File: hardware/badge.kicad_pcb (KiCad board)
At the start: 2 copper layers, 88 x 156.6 mm, 130 parts, among them J1 Micro_SD_Card, J2 MY-18650-01, J3 Conn_01x40, J4 USB_C_Receptacle_USB2.0_14P, J5 MY-18650-01, Q1 AO3400A, Q3 AO3400A, SW1 SW_Push, SW10 SW_Push, SW11 SW_Push, SW12 SW_Push, SW13 SW_Push, SW14 SW_Push, SW15 SW_Push, SW16 SW_Push, SW17 SW_Push, SW18 SW_Push, SW19 SW_Push, SW2 SW_Push, SW20 SW_Push, SW21 SW_Push, SW22 SW_Push, SW23 SW_Push, SW25 SW_Push, SW26 SW_Push, SW27 SW_Push, SW28 SW_Push, SW29 SW_Push, SW3 SW_Push, SW30 SW_Push, SW31 SW_Push, SW33 SW_Push, SW34 SW_Push, SW35 SW_Push, SW36 SW_Push, SW37 SW_Push, SW38 SW_Push, SW39 SW_Push, SW4 SW_Push, SW5 SW_Push, SW57 MK-12C02-G020, SW58 SKRHABE010, SW6 SW_Push, SW7 SW_Push, SW8 BOOT, SW9 SW_Push, U1 ESP32-S3-WROOM-1, U10 PCA9555PW, U11 PCA9555PW, U3 BQ24075RGT, U4 TLV62569DBV, U5 BME280, U6 USBLC6-2P6, U7 BMI270, U8 Ai-Thinker-Ra-02, U9 MAX98357A

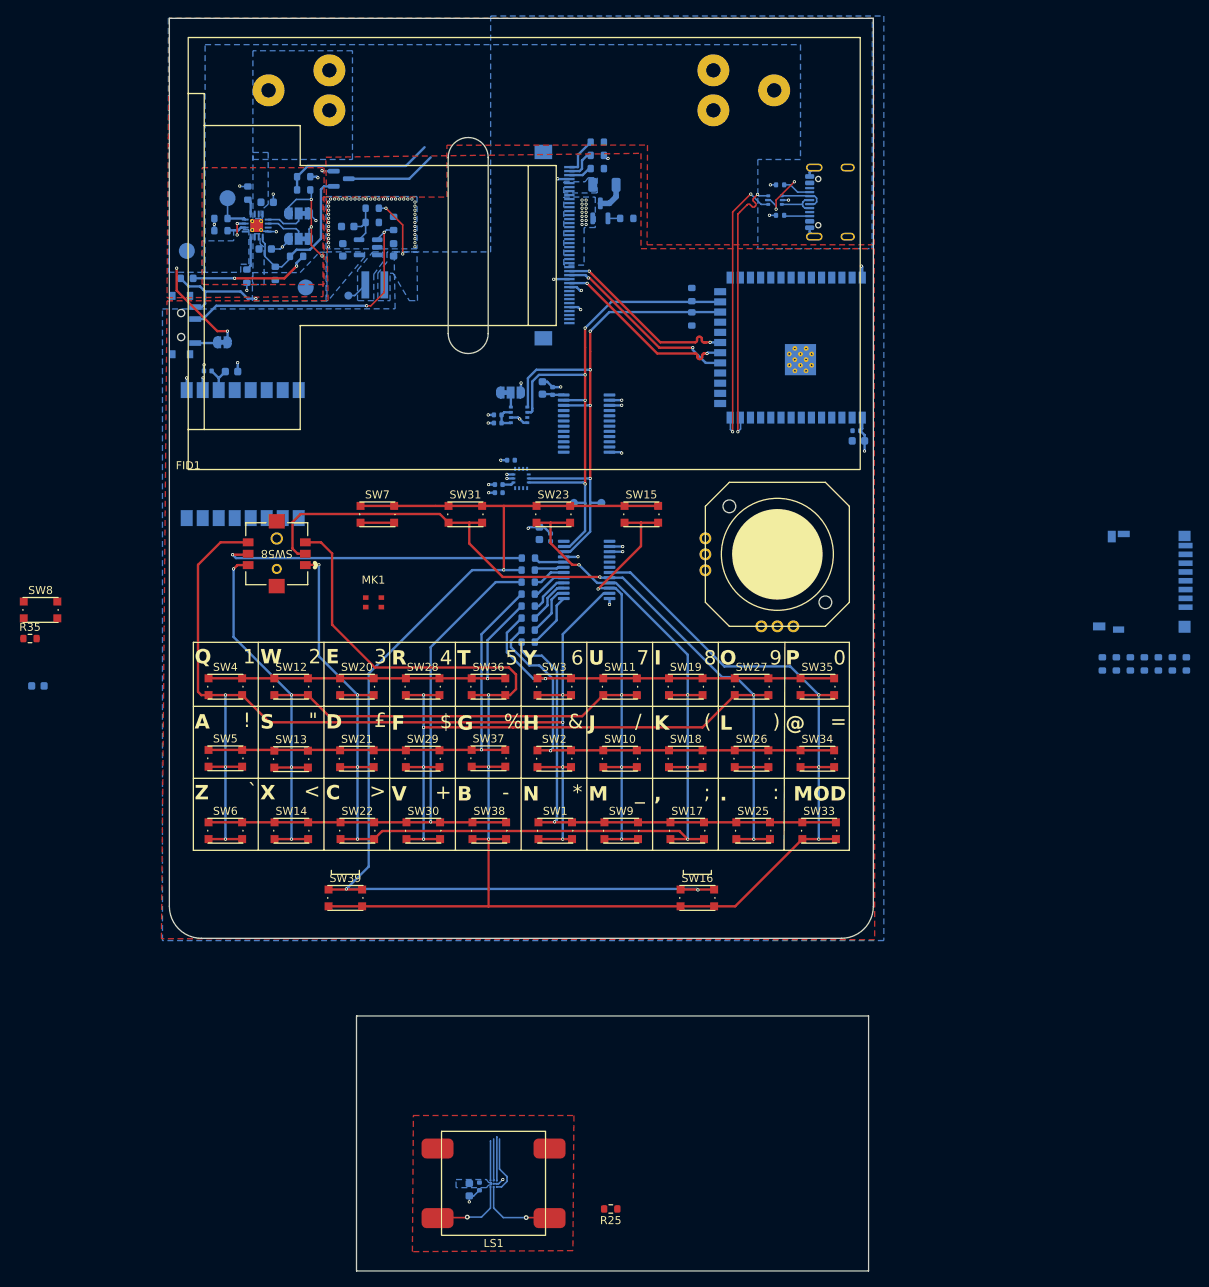
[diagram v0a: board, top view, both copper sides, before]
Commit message: Add sdcard fooprint
Remove io expander
Reorganize a bit the mcu schematic
Routed audio
Routed lora
Partial pin swapping of esp32 for facilitating routing
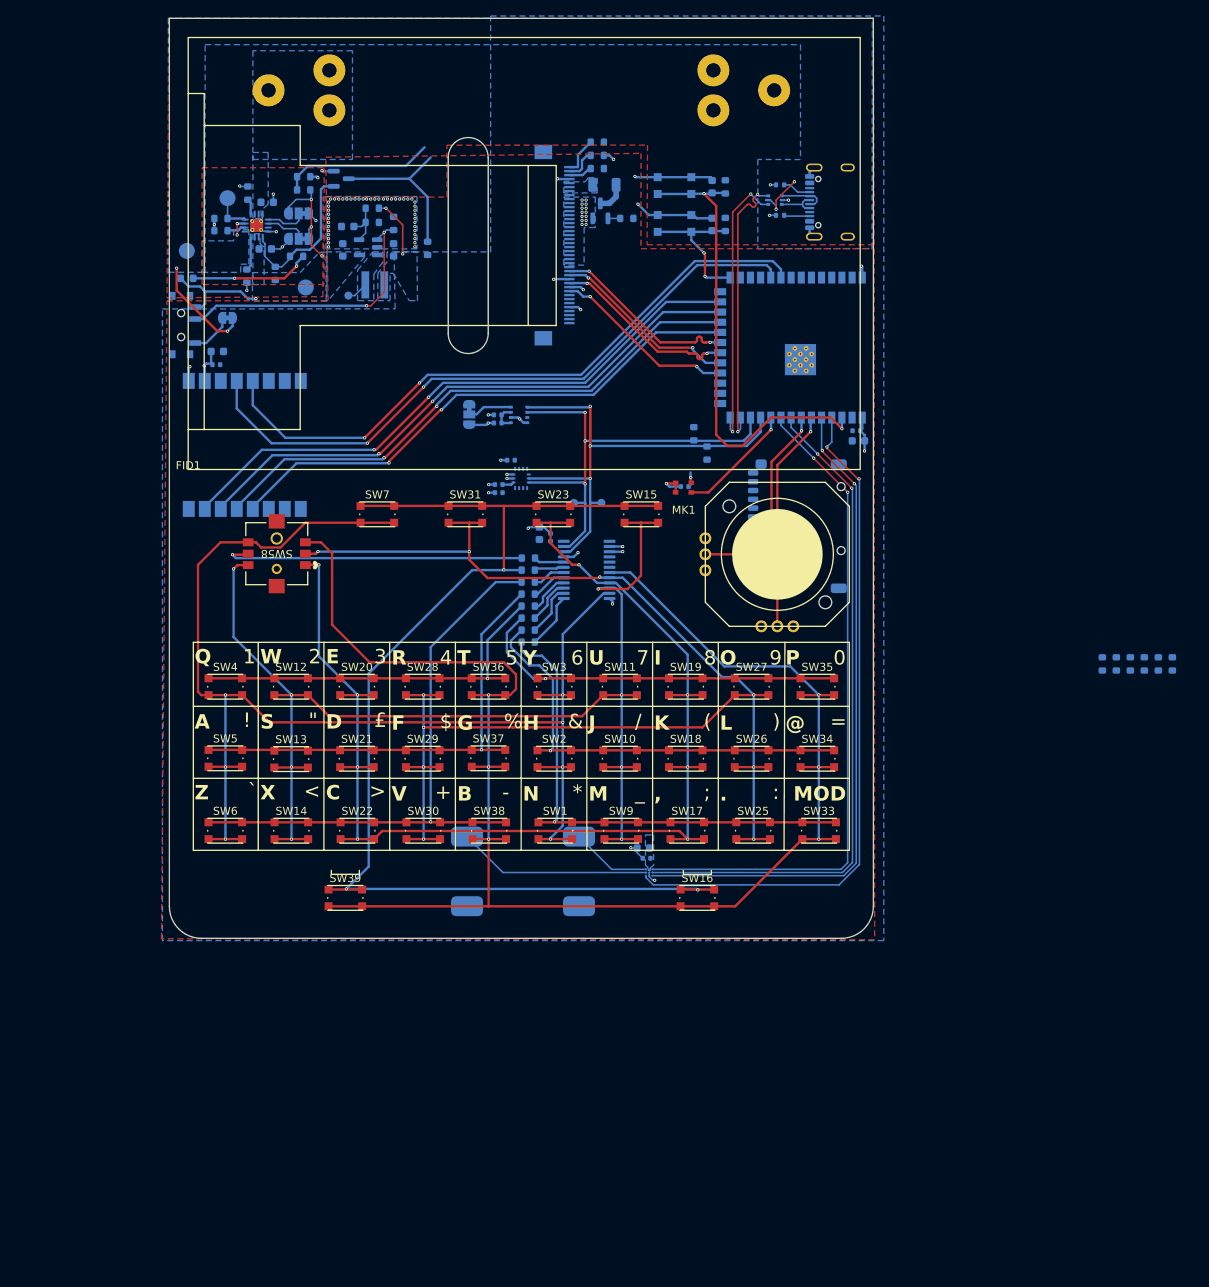
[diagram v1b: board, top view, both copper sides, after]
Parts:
- removed J1: Micro_SD_Card, Connector_Card:microSD_HC_Hirose_DM3D-SF
- removed R1: 10k, Resistor_SMD:R_0603_1608Metric
- removed U10: PCA9555PW, Package_SO:TSSOP-24_4.4x7.8mm_P0.65mm
- removed U8: Ai-Thinker-Ra-02, RF_Module:Ai-Thinker-Ra-01-LoRa
- added J6: Micro_SD_Card_Det1, badge:TF-01A, B.Cu at (164.7, 94.5)
- added R38: 10k, Resistor_SMD:R_0603_1608Metric, B.Cu at (150.5, 52.1)
- added SW24: BOOT, badge:bottonepiccolo_C2888430, B.Cu at (144.1, 56.6)
- added U2: Ai-Thinker-Ra-02, RF_Module:Ai-Thinker-Ra-01-LoRa, B.Cu at (90.4, 84.3)
- C11: value 100nF 6.3V -> 10uF; footprint Capacitor_SMD:C_0402_1005Metric -> Capacitor_SMD:C_0603_1608Metric
- C12: value 10uF -> 100nF 6.3V; footprint Capacitor_SMD:C_0603_1608Metric -> Capacitor_SMD:C_0402_1005Metric
- LS1, R25, R35: moved to B.Cu
- SW8: value BOOT -> RST; moved to B.Cu
- moved R25 122.2 mm to (113.3, 59.8), turned to -90 degrees
- moved C15 104.9 mm to (148.8, 52.0), turned to 90 degrees
- moved R35 101.2 mm to (150.5, 56.8), turned to -90 degrees
- moved SW8 95.4 mm to (144.1, 51.9), turned to 180 degrees
- moved C13 47.9 mm to (140.2, 134.7), turned to 180 degrees
- moved C14 46.0 mm to (140.7, 136.0), turned to 180 degrees
- moved U9 43.5 mm to (141.0, 137.8), turned to 180 degrees
- moved MK1 41.4 mm to (145.3, 89.7), turned to 180 degrees
- moved LS1 39.2 mm to (125.2, 137.6)
- moved C16 29.5 mm to (148.8, 56.8)
- moved C17 20.4 mm to (145.4, 89.5), turned to 180 degrees
- moved R36 17.4 mm to (146.6, 82.9)
- moved R37 16.9 mm to (148.2, 85.3)
- moved JP4 5.84 mm to (118.5, 80.5), turned to -90 degrees
- moved JP3 3.11 mm to (88.3, 68.5)
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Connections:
- C15 pad 1: Net-(U1-IO0) -> /mcu/RST
- C16 pad 1: +3.3V -> /mcu/BOOT
- LS1 pad 1: Net-(U9-OUTP) -> Net-(U9-OUTN)
- LS1 pad 2: Net-(U9-OUTN) -> Net-(U9-OUTP)
- MK1 pad 1: /mcu/MICROPHONE -> /mcu/MIC
- R35 pad 2: Net-(U1-IO0) -> /mcu/BOOT
- R36 pad 2: /imu/SDA -> /mcu/SDA
- R37 pad 2: /imu/SCL -> /mcu/SCL
- SW8 pad 2: Net-(U1-IO0) -> /mcu/RST
- TP5 pad 1: /imu/SCL -> /mcu/SCL
- TP6 pad 1: /imu/SDA -> /mcu/SDA
- U1 pad 10: /mcu/VBAT_DIV2 -> /mcu/MIC
- U1 pad 11: /mcu/LORA_IRQ -> /mcu/SCL
- U1 pad 12: unconnected-(U1-IO8-Pad12) -> /mcu/SDA
- U1 pad 15: /mcu/SD_D0 -> unconnected-(U1-IO3-Pad15)
- U1 pad 22: /AUDIO.BCLK -> /LORA.CLK
- U1 pad 23: unconnected-(U1-IO21-Pad23) -> /LORA.MISO
- U1 pad 24: /imu/SCL -> /LORA.MOSI
- U1 pad 25: /imu/SDA -> /LORA.CS
- U1 pad 27: Net-(U1-IO0) -> /mcu/BOOT
- U1 pad 3: Net-(U1-EN) -> /mcu/RST
- U1 pad 31: unconnected-(U1-IO38-Pad31) -> /mcu/LORA_CE
- U1 pad 32: unconnected-(U1-IO39-Pad32) -> /mcu/LORA_IRQ
- U1 pad 35: Net-(U1-IO42) -> unconnected-(U1-IO42-Pad35)
- U1 pad 38: /mcu/SD_CLK -> unconnected-(U1-IO2-Pad38)
- U1 pad 39: /mcu/SD_CMD -> unconnected-(U1-IO1-Pad39)
- U1 pad 4: /mcu/CHG -> /AUDIO.LRCLK
- U1 pad 5: unconnected-(U1-IO5-Pad5) -> /AUDIO.BCLK
- U1 pad 6: unconnected-(U1-IO6-Pad6) -> /mcu/YOUT
- U1 pad 7: /mcu/MICROPHONE -> /mcu/XOUT
- U1 pad 8: /AUDIO.LRCLK -> /AUDIO.SD
- U1 pad 9: /AUDIO.SD -> /mcu/MUTE
- U11 pad 1: unconnected-(U11-~{INT}-Pad1) -> /keyboard/IO_IRQ
- U11 pad 22: /imu/SCL -> /mcu/SCL
- U11 pad 23: /imu/SDA -> /mcu/SDA
- U5 pad 3: /imu/SDA -> /mcu/SDA
- U5 pad 4: /imu/SCL -> /mcu/SCL
- U7 pad 13: /imu/SCL -> /mcu/SCL
- U7 pad 14: /imu/SDA -> /mcu/SDA
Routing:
- net /mcu/LORA_CE: track 0.00 -> 82.5 mm, vias 0 -> 2
- net /mcu/LORA_IRQ: track 0.00 -> 81.4 mm, vias 0 -> 2
- net /AUDIO.SD: track 5.21 -> 84.3 mm, vias 0 -> 2
- net /AUDIO.LRCLK: track 7.27 -> 86.2 mm, vias 0 -> 2
- net /mcu/MUTE: track 4.96 -> 83.8 mm, vias 0 -> 2
- net /AUDIO.BCLK: track 5.47 -> 83.6 mm, vias 0 -> 2
- net /LORA.CS: track 0.00 -> 75.3 mm, vias 0 -> 2
- net /LORA.MOSI: track 0.00 -> 72.8 mm, vias 0 -> 2
- net /imu/SCL: track 70.9 -> 0.00 mm, vias 4 -> 0
- net /LORA.MISO: track 0.00 -> 70.4 mm, vias 0 -> 2
- net /imu/SDA: track 69.7 -> 0.00 mm, vias 4 -> 0
- net /LORA.CLK: track 0.00 -> 67.8 mm, vias 0 -> 2
- net /mcu/SCL: track 0.00 -> 65.8 mm, vias 0 -> 3
- net /mcu/RST: track 0.00 -> 59.4 mm, vias 0 -> 2
- net /mcu/SDA: track 0.00 -> 57.3 mm, vias 0 -> 3
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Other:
- board size 88 x 156.6 mm -> 88 x 115 mm

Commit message: Route all board
Fix CS missing for SD card
Add IMU symbol and footprint to the project lib
Finish esp32 pinswaps
Move non critical signals to the keyboard IO expander
Add power flag symbols
Fix Dpad pin type
Fix IMU pin type
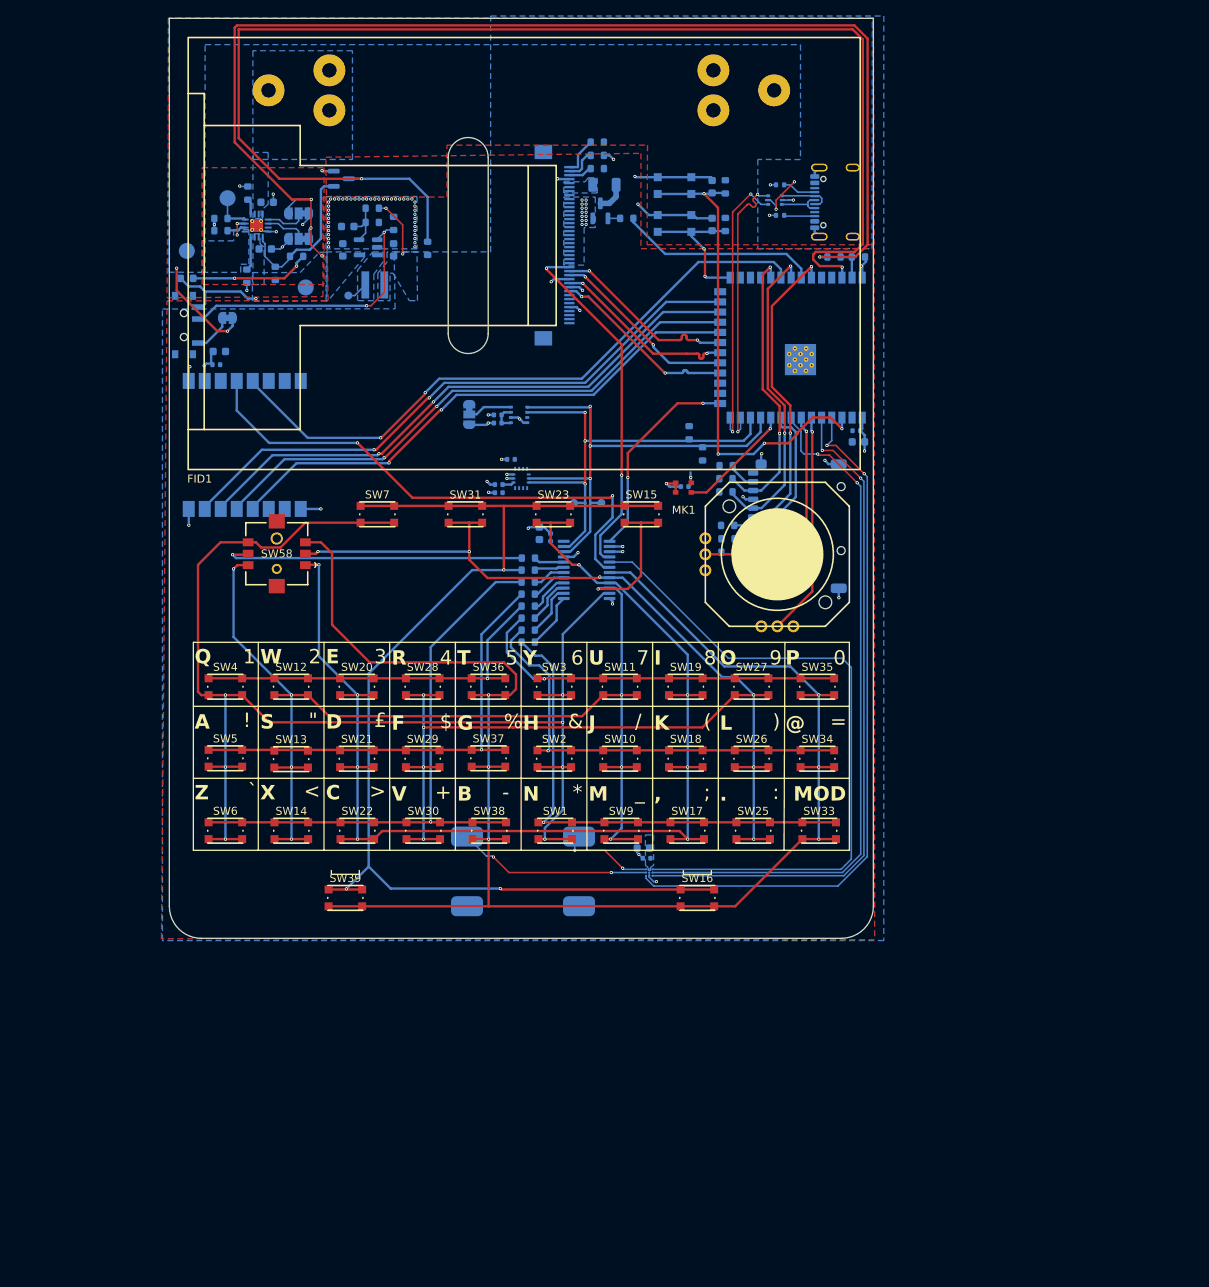
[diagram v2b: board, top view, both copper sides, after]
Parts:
- TP5: value TestPoint -> SCL
- TP6: value TestPoint -> SDA
- U7: footprint footprints:BMI270_BOS -> badge:BMI270_BOS
- moved R33 70.1 mm to (167.1, 60.8)
- moved R34 66.8 mm to (164.1, 60.8), turned to 0 degrees
- moved R2 61.0 mm to (150.6, 86.9), turned to 0 degrees
- moved R3 58.8 mm to (150.6, 88.5), turned to 0 degrees
- moved R4 56.6 mm to (150.6, 90.2), turned to 0 degrees
- moved R5 53.2 mm to (150.8, 94.4), turned to 0 degrees
- moved R6 51.0 mm to (150.8, 96.1), turned to 0 degrees
- moved R7 48.8 mm to (150.8, 97.7), turned to 0 degrees
- moved J4 0.64 mm to (165.4, 54.0)
- moved R36 0.60 mm to (146.0, 82.8)
- moved R37 0.57 mm to (147.7, 85.4)
- moved SW57 0.35 mm to (83.2, 69.3)
- moved C11 0.25 mm to (87.2, 72.6)
- moved C18 0.13 mm to (167.1, 83.9)
- moved C10 0.10 mm to (123.7, 86.1)
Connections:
- J3 pad 15: /lcd/RESET -> /keyboard/LCD_RESET
- J6 pad 2: Net-(J6-DAT3/CD) -> /mcu/SD_CS
- R6 pad 2: Net-(J6-DAT3/CD) -> /mcu/SD_CS
- U1 pad 15: unconnected-(U1-IO3-Pad15) -> /keyboard/IO_IRQ
- U1 pad 31: /mcu/LORA_CE -> /mcu/SD_D0
- U1 pad 33: unconnected-(U1-IO40-Pad33) -> /mcu/SD_CLK
- U1 pad 34: unconnected-(U1-IO41-Pad34) -> /lcd/BACKLIGHT
- U1 pad 35: unconnected-(U1-IO42-Pad35) -> /mcu/SD_CMD
- U1 pad 38: unconnected-(U1-IO2-Pad38) -> /mcu/CHG
- U1 pad 39: unconnected-(U1-IO1-Pad39) -> /mcu/VBAT_DIV2
- U1 pad 9: /mcu/MUTE -> /mcu/SD_CS
- U11 pad 4: unconnected-(U11-IO0_0-Pad4) -> /keyboard/LCD_RESET
- U11 pad 5: unconnected-(U11-IO0_1-Pad5) -> /audio/MUTE
- U11 pad 6: unconnected-(U11-IO0_2-Pad6) -> /keyboard/LORA_CE
- U2 pad 4: /mcu/LORA_CE -> /keyboard/LORA_CE
- U3 pad 7: /power/~{PGOOD} -> unconnected-(U3-~{PGOOD}-Pad7)
- U9 pad A1: /mcu/MUTE -> /audio/MUTE
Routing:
- net /mcu/CHG: track 20.2 -> 164.3 mm, vias 0 -> 2
- net VSYS: track 27.9 -> 166.7 mm, vias 4 -> 5
- net /audio/MUTE: track 0.00 -> 85.0 mm
- net /mcu/MUTE: track 83.8 -> 0.00 mm, vias 2 -> 0
- net /mcu/LORA_CE: track 82.5 -> 0.00 mm, vias 2 -> 0
- net /keyboard/LORA_CE: track 0.00 -> 66.3 mm, vias 0 -> 2
- net /keyboard/LCD_RESET: track 0.00 -> 44.9 mm, vias 0 -> 2
- net /mcu/SD_CMD: track 0.00 -> 41.5 mm, vias 0 -> 2
- net /mcu/SD_CLK: track 0.00 -> 39.6 mm, vias 0 -> 2
- net /mcu/SD_D0: track 0.00 -> 35.9 mm, vias 0 -> 2
- net /keyboard/IO_IRQ: track 0.00 -> 26.1 mm, vias 0 -> 2
- net /lcd/BACKLIGHT: track 0.00 -> 25.0 mm
- net /mcu/SD_CS: track 0.00 -> 21.2 mm
- net /mcu/VBAT_DIV2: track 19.1 -> 3.99 mm
- net GND: track 88.8 -> 103.0 mm, vias 98 -> 104
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
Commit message: Associate all LCSC component
Change sdcard pullup resistor to 47K
Center main schematic
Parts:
- R17, R36, R37: value 1.2k -> 1.2K
- R18: value 1.78k -> 1.78K
- R19, R2, R20, R24, R25, R3, R35, R38, R4, R5, R6, R7: value 10k -> 47K
- R21: value 680k -> 680K
- R23: value 330 -> 330R
- R26, R27: value 5k1 -> 5.1K
